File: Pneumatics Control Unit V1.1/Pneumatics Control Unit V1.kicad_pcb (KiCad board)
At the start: 2 copper layers, 75 parts, among them J1 RX_PORT, J10 Conn_01x02_Male, J11 Conn_01x02_Male, J12 10118194-0001LF, J2 RX_PORT, J3 MICROMOD-2222, J4 Conn_01x02_Male, J5 Conn_01x02_Male, J6 Conn_01x02_Male, J7 Conn_01x02_Male, J8 Conn_01x02_Male, J9 Conn_01x02_Male, U1 ISL83490IBZ, U2 MIC2178-3.3YWM, U4 MC78M05CDTRKG

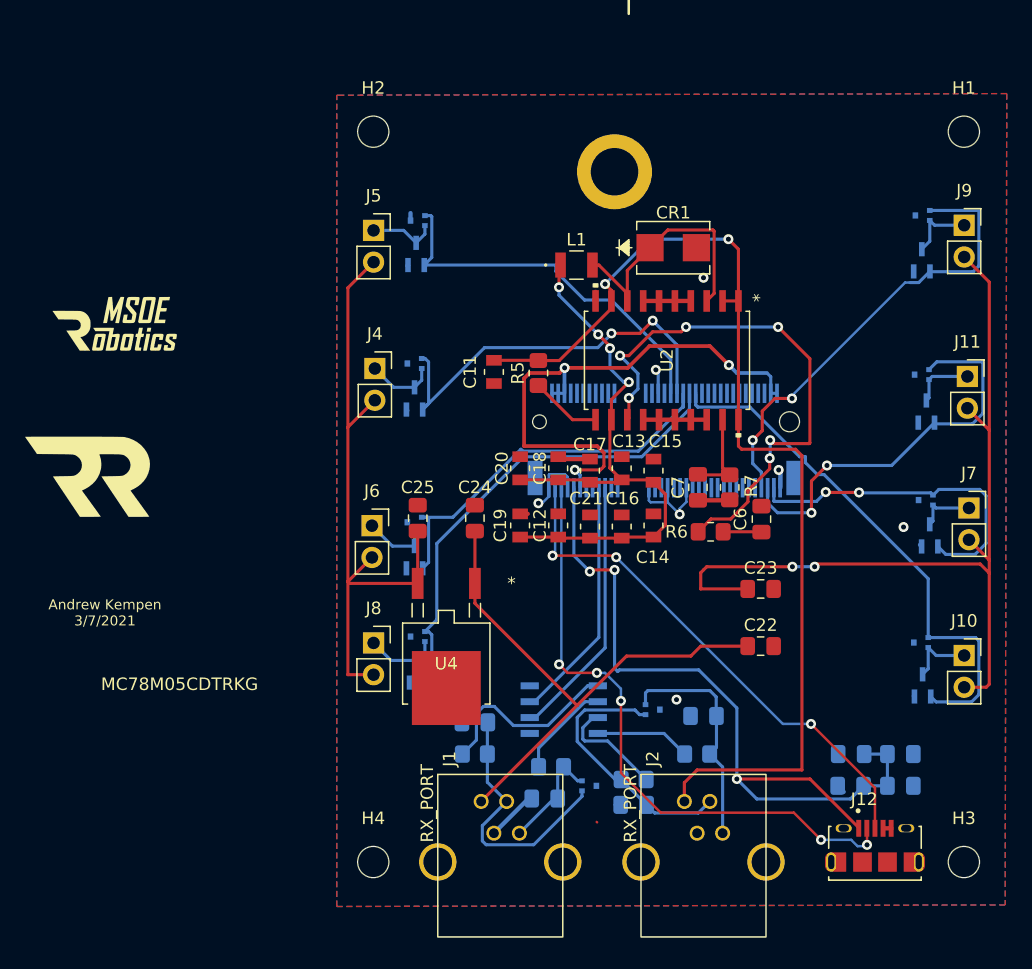
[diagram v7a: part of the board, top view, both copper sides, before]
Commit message: Fixing the PCB silkscreen
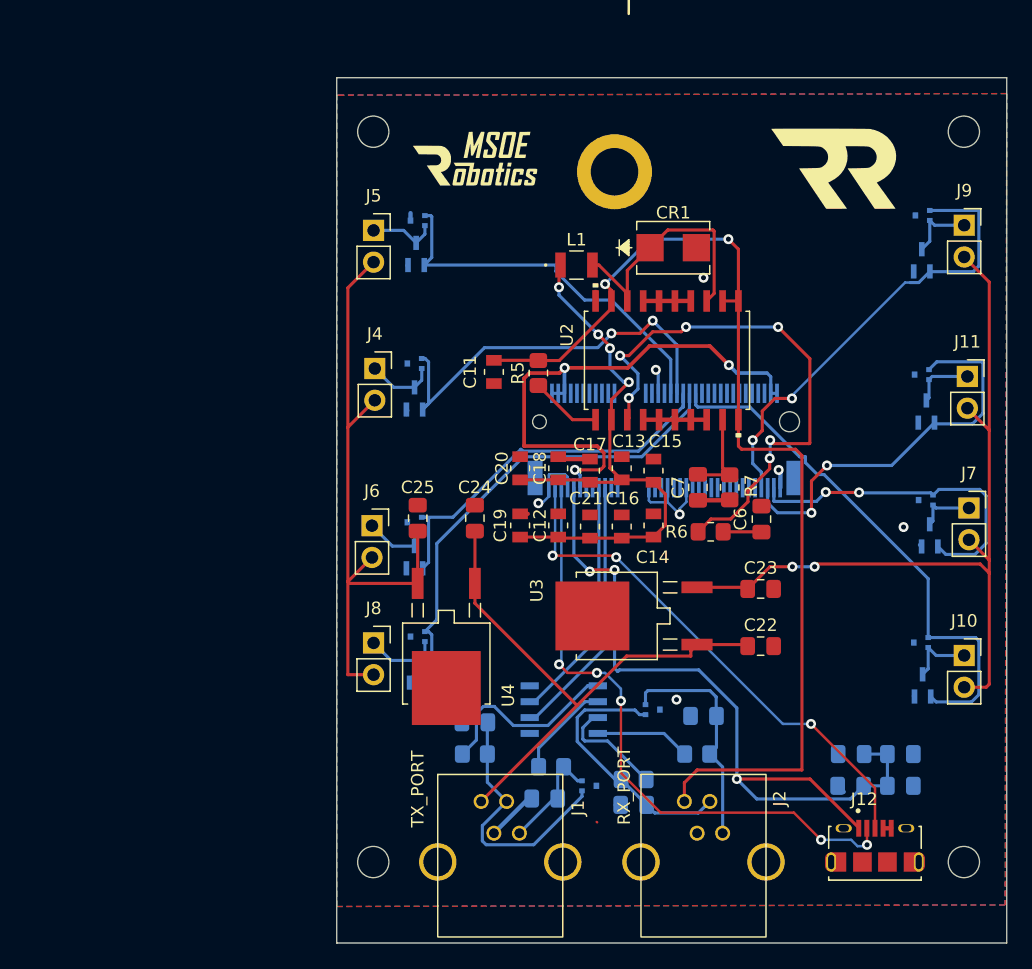
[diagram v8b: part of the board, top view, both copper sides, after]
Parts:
- added U3: MC78M05CDTRKG, 12v5v:MC78M05CDTRKG, F.Cu at (126.2, 107.3)
- J1: value RX_PORT -> TX_PORT
- moved G*** 64.6 mm to (143.6, 71.5)
- moved G*** 57.8 mm to (143.0, 74.5)
- moved G*** 31.7 mm to (114.8, 70.7)
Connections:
- C25 pad 1: 5V -> 5V_L
- J4 pad 2: 5V -> 5V_L
- J5 pad 2: 5V -> 5V_L
- J6 pad 2: 5V -> 5V_L
- J8 pad 2: 5V -> 5V_L
- U4 pad 3: 5V -> 5V_L
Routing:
- net 5V: track 122.1 -> 66.5 mm
- net 5V_L: track 0.00 -> 51.5 mm
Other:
- board outline added: 53.6 x 69.2 mm
- board text added: "Andrew Kempen Asher Sprigler Nathan Roth 4/5/2022"
- board text removed: "Andrew Kempen 3/7/2021"
- board text removed: "JLCJLCJLCJLC"
